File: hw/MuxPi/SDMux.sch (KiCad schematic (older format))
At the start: 14 parts, among them J2 112K-TBA0-RA1, P9 T821108A1S100CEU, Q4 MMBT4403LT1, Q5 MMBT4403LT1, U7 MC74HC1G04DTT1G, U8 TS3A27518EPWR

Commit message: Add detailed info to MuxPi electronic components
The additional information includes manufacturer names and
manufacturer symbols for all components except ceramic capacitors
and resistors. It allows to create BOM (Bill Of Materials) with
actual product names.

Change-Id: Id1c518bba60322d4b8b132ad14261806070abc27
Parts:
- C26: Manufacturer (none) -> AVX; Symbol (none) -> TAJA475K016RNJ
- J2: Manufacturer (none) -> ATTEND; Symbol (none) -> 112K-TBA0-RA1
- P9: Manufacturer (none) -> AMPHENOL; Symbol (none) -> T821108A1S100CEU
- Q4, Q5: Manufacturer (none) -> ON SEMICONDUCTOR; Symbol (none) -> MMBT4403LT1G
- U7: Manufacturer (none) -> ON SEMICONDUCTOR; Symbol (none) -> MC74HC1G04DTT1G
- U8: Manufacturer (none) -> TEXAS INSTRUMENTS; Symbol (none) -> TS3A27518EPWR
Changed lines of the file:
@@
 F 3 "http://www.ti.com/lit/ds/symlink/ts3a27518e.pdf" H 5350 4650 60  0001 C CNN
 F 4 "http://pl.farnell.com/texas-instruments/ts3a27518epwr/ic-6bit-1-of-2-mux-demux-24tssop/dp/1735605" H 5050 4950 60  0001 C CNN "Shop link"
+F 5 "TEXAS INSTRUMENTS" H 5050 4950 50  0001 C CNN "Manufacturer"
+F 6 "TS3A27518EPWR" H 5050 4950 50  0001 C CNN "Symbol"
 	1    5050 4950
 	1    0    0    -1
@@
 F 3 "http://www.tme.eu/pl/Document/0bd9f377abd5f258bb30856efe9f427e/mc74hc1g04.pdf" H 4095 3365 60  0001 C CNN
 F 4 "http://www.tme.eu/pl/details/mc74hc1g04dtt1g/bramki-inwertery/on-semiconductor/" H 3950 3250 60  0001 C CNN "Shop link"
+F 5 "ON SEMICONDUCTOR" H 3950 3250 50  0001 C CNN "Manufacturer"
+F 6 "MC74HC1G04DTT1G" H 3950 3250 50  0001 C CNN "Symbol"
 	1    3950 3250
 	1    0    0    -1
@@
 F 3 "http://www.tme.eu/pl/Document/d9baf2fd66256bac7b840e9a66d44492/112K-TBA0-RA1.pdf" H 6900 4250 60  0001 C CNN
 F 4 "http://www.tme.eu/pl/details/112k-tba0-ra1/zlacza-do-kart/attend/" H 6900 4250 60  0001 C CNN "Shop link"
+F 5 "ATTEND" H 6900 4250 50  0001 C CNN "Manufacturer"
+F 6 "112K-TBA0-RA1" H 6900 4250 50  0001 C CNN "Symbol"
 	1    6900 4250
 	1    0    0    -1
@@
 F 3 "http://www.tme.eu/pl/Document/85f84849ee9dc6997647a15c8c95a9d3/taj.pdf" H 7850 5850 60  0001 C CNN
 F 4 "http://www.tme.eu/pl/details/taja475k016r/kondensatory-tantalowe-smd/avx/taja475k016rnj/" H 7850 5850 60  0001 C CNN "Shop link"
+F 5 "AVX" H 7850 5850 50  0001 C CNN "Manufacturer"
+F 6 "TAJA475K016RNJ" H 7850 5850 50  0001 C CNN "Symbol"
 	1    7850 5850
 	1    0    0    -1
@@
 F 3 "http://www.tme.eu/pl/Document/cda30bae7de800ca9be388e3f3476120/T821-1-08-S1.pdf" H 8850 700 60  0001 C CNN
 F 4 "http://www.tme.eu/pl/details/t821-1-08-s1/zlacza-idc/amphenol/t821108a1s100ceu/" H 8850 1900 60  0001 C CNN "Shop link"
+F 5 "AMPHENOL" H 8850 1900 50  0001 C CNN "Manufacturer"
+F 6 "T821108A1S100CEU" H 8850 1900 50  0001 C CNN "Symbol"
 	1    8850 1900
 	1    0    0    -1
@@
 F 3 "https://www.tme.eu/pl/Document/b8fb0b2a2196eb2b0100116bda4d5a47/mmbt4403.pdf" H 5400 1600 50  0001 L CNN
 F 4 "https://www.tme.eu/pl/details/mmbt4403lt1g/tranzystory-pnp-smd/on-semiconductor/" V 5400 1600 50  0001 C CNN "Shop link"
+F 5 "ON SEMICONDUCTOR" V 5400 1600 50  0001 C CNN "Manufacturer"
+F 6 "MMBT4403LT1G" V 5400 1600 50  0001 C CNN "Symbol"
 	1    5400 1600
-	0    1    -1   0
-$EndComp
-$Comp
-L MuxPi:MMBT4403LT1 Q5
-U 1 1 5A6A2FE1
-P 5400 2650
-F 0 "Q5" V 5728 2650 50  0000 C CNN
-F 1 "MMBT4403LT1" V 5637 2650 50  0000 C CNN
-F 2 "TO_SOT_Packages_SMD:SOT-23" H 5600 2575 50  0001 L CIN
-F 3 "https://www.tme.eu/pl/Document/b8fb0b2a2196eb2b0100116bda4d5a47/mmbt4403.pdf" H 5400 2650 50  0001 L CNN
-F 4 "https://www.tme.eu/pl/details/mmbt4403lt1g/tranzystory-pnp-smd/on-semiconductor/" V 5400 2650 50  0001 C CNN "Shop link"
-	1    5400 2650
 	0    1    -1   0
 $EndComp
@@
 	5400 2200 5400 1850
 Connection ~ 5400 1850
+$Comp
+L MuxPi:MMBT4403LT1 Q5
+U 1 1 5A8F3224
+P 5400 2650
+F 0 "Q5" V 5728 2650 50  0000 C CNN
+F 1 "MMBT4403LT1" V 5637 2650 50  0000 C CNN
+F 2 "TO_SOT_Packages_SMD:SOT-23" H 5600 2575 50  0001 L CIN
+F 3 "https://www.tme.eu/pl/Document/b8fb0b2a2196eb2b0100116bda4d5a47/mmbt4403.pdf" H 5400 2650 50  0001 L CNN
+F 4 "https://www.tme.eu/pl/details/mmbt4403lt1g/tranzystory-pnp-smd/on-semiconductor/" V 5400 2650 50  0001 C CNN "Shop link"
+F 5 "ON SEMICONDUCTOR" V 5400 2650 50  0001 C CNN "Manufacturer"
+F 6 "MMBT4403LT1G" V 5400 2650 50  0001 C CNN "Symbol"
+	1    5400 2650
+	0    1    -1   0
+$EndComp
 $EndSCHEMATC

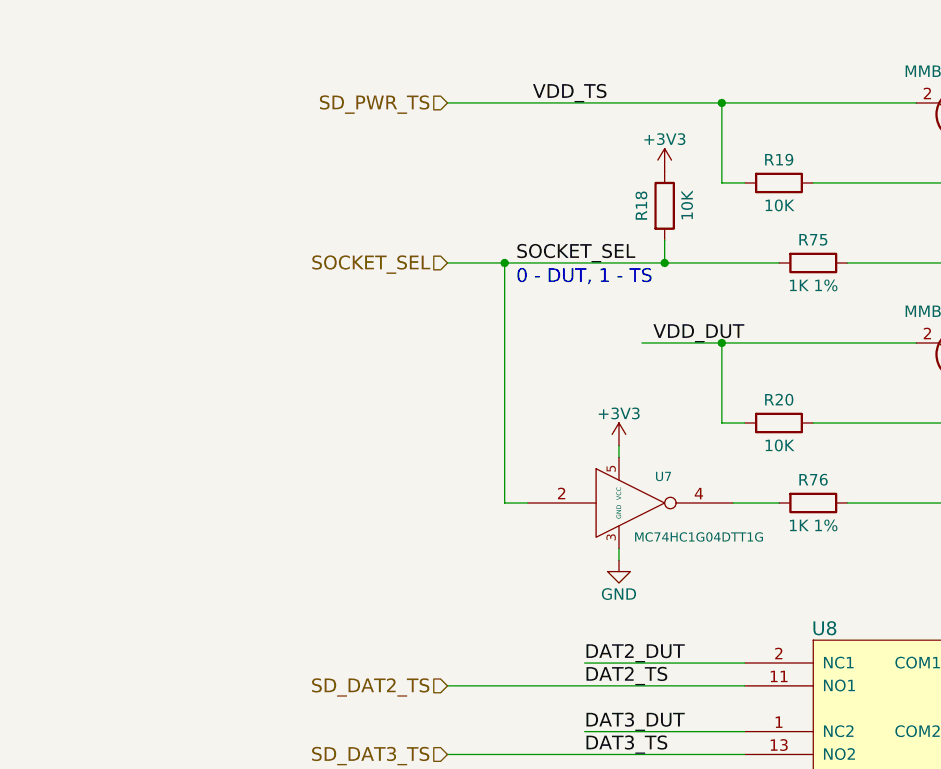
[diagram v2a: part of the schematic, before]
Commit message: Update hardware design to version 1.2
Change-Id: I36445887bfaa5fada88d8bf3915603605de47512
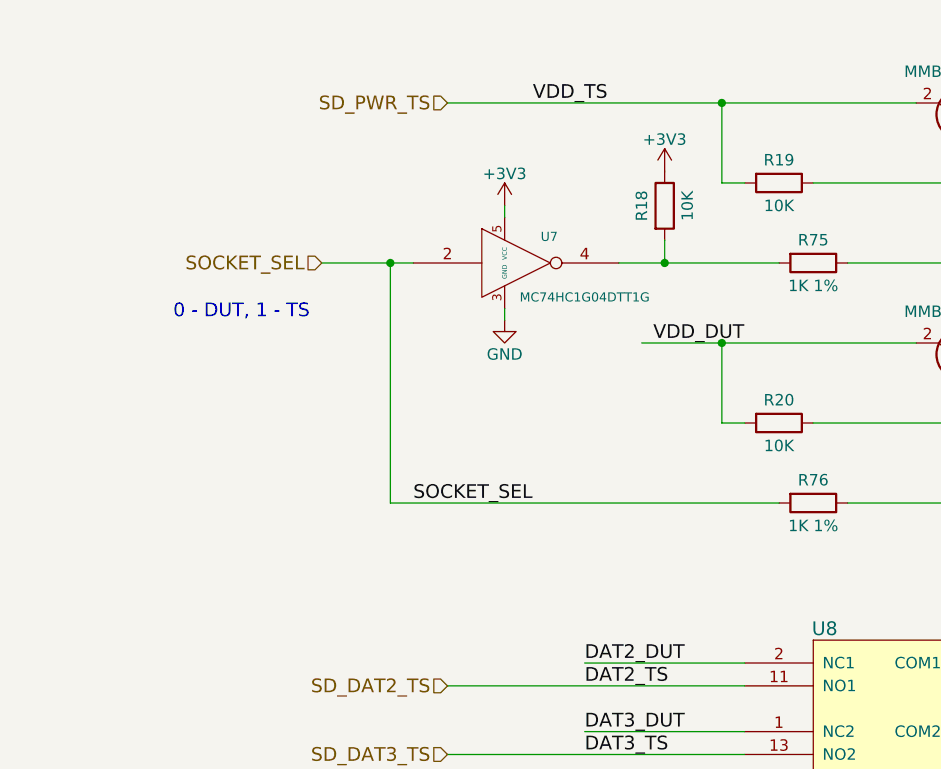
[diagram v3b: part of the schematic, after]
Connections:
- net SOCKET_SEL: now also R76.2; no longer R18.2, R75.2
- net at U7.4: now also R18.2, R75.2; no longer R76.2
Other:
- moved on the sheet: U7
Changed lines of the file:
@@
 EESchema Schematic File Version 4
+LIBS:MuxPi-cache
 EELAYER 26 0
 EELAYER END
@@
 encoding utf-8
 Sheet 7 12
-Title ""
-Date ""
-Rev ""
-Comp ""
-Comment1 ""
-Comment2 ""
+Title "MuxPi"
+Date "2018-04-20"
+Rev "1.2"
+Comp "SRPOL"
+Comment1 "Author: Adam Malinowski <a.malinowsk2@partner.samsung.com>"
+Comment2 "Copyright (c) 2016 - 2018 Samsung Electronics Co., Ltd All Rights Reserved"
 Comment3 ""
 Comment4 ""
@@
 L MuxPi:74AHC1G14 U7
 U 1 1 584BAD12
-P 3950 3250
+P 3450 2200
 AR Path="/584BAD12" Ref="U7"  Part="1"
 AR Path="/584BA053/584BAD12" Ref="U7"  Part="1"
-F 0 "U7" H 4095 3365 40  0000 C CNN
-F 1 "MC74HC1G04DTT1G" H 4250 3100 40  0000 C CNN
-F 2 "TO_SOT_Packages_SMD:SOT-23-5" H 4045 3115 30  0001 C CNN
-F 3 "http://www.tme.eu/pl/Document/0bd9f377abd5f258bb30856efe9f427e/mc74hc1g04.pdf" H 4095 3365 60  0001 C CNN
-F 4 "http://www.tme.eu/pl/details/mc74hc1g04dtt1g/bramki-inwertery/on-semiconductor/" H 3950 3250 60  0001 C CNN "Shop link"
-F 5 "ON SEMICONDUCTOR" H 3950 3250 50  0001 C CNN "Manufacturer"
-F 6 "MC74HC1G04DTT1G" H 3950 3250 50  0001 C CNN "Symbol"
-	1    3950 3250
+F 0 "U7" H 3595 2315 40  0000 C CNN
+F 1 "MC74HC1G04DTT1G" H 3750 2050 40  0000 C CNN
+F 2 "TO_SOT_Packages_SMD:SOT-23-5" H 3545 2065 30  0001 C CNN
+F 3 "http://www.tme.eu/pl/Document/0bd9f377abd5f258bb30856efe9f427e/mc74hc1g04.pdf" H 3595 2315 60  0001 C CNN
+F 4 "http://www.tme.eu/pl/details/mc74hc1g04dtt1g/bramki-inwertery/on-semiconductor/" H 3450 2200 60  0001 C CNN "Shop link"
+F 5 "ON SEMICONDUCTOR" H 3450 2200 50  0001 C CNN "Manufacturer"
+F 6 "MC74HC1G04DTT1G" H 3450 2200 50  0001 C CNN "Symbol"
+	1    3450 2200
 	1    0    0    -1
 $EndComp
 Text Label 4050 2550 0    60   ~ 0
 VDD_DUT
-Text Notes 3450 2300 0    60   ~ 0
+Text Notes 1950 2450 0    60   ~ 0
 0 - DUT, 1 - TS
 $Comp
@@
 L MuxPi:GND #PWR082
 U 1 1 584BAD22
-P 3900 3500
-F 0 "#PWR082" H 3900 3250 50  0001 C CNN
-F 1 "GND" H 3900 3350 50  0000 C CNN
-F 2 "" H 3900 3500 60  0000 C CNN
-F 3 "" H 3900 3500 60  0000 C CNN
-	1    3900 3500
+P 3400 2450
+F 0 "#PWR082" H 3400 2200 50  0001 C CNN
+F 1 "GND" H 3400 2300 50  0000 C CNN
+F 2 "" H 3400 2450 60  0000 C CNN
+F 3 "" H 3400 2450 60  0000 C CNN
+	1    3400 2450
 	-1   0    0    -1
 $EndComp
@@
 L MuxPi:+3V3 #PWR081
 U 1 1 584BAD80
-P 3900 3000
-F 0 "#PWR081" H 3900 2850 50  0001 C CNN
-F 1 "+3V3" H 3900 3140 50  0000 C CNN
-F 2 "" H 3900 3000 60  0000 C CNN
-F 3 "" H 3900 3000 60  0000 C CNN
-	1    3900 3000
-	1    0    0    -1
-$EndComp
-Text Label 3450 2200 0    60   ~ 0
+P 3400 1950
+F 0 "#PWR081" H 3400 1800 50  0001 C CNN
+F 1 "+3V3" H 3400 2090 50  0000 C CNN
+F 2 "" H 3400 1950 60  0000 C CNN
+F 3 "" H 3400 1950 60  0000 C CNN
+	1    3400 1950
+	1    0    0    -1
+$EndComp
+Text Label 3000 3250 0    60   ~ 0
 SOCKET_SEL
 $Comp
@@
 Text Label 7500 5550 0    60   ~ 0
 USD_VDD
-Text HLabel 3150 2200 0    60   Input ~ 0
+Text HLabel 2600 2200 0    60   Input ~ 0
 SOCKET_SEL
 Text HLabel 3150 1500 0    60   Input ~ 0
@@
 	4350 5950 4350 6050
 Wire Wire Line
-	3900 3450 3900 3500
-Wire Wire Line
-	3900 3000 3900 3050
+	3400 2400 3400 2450
+Wire Wire Line
+	3400 1950 3400 2000
 Wire Wire Line
 	4450 5450 3750 5450
@@
 Wire Wire Line
 	9200 1950 9200 2150
-Connection ~ 4100 2200
 Wire Wire Line
 	3750 5750 4350 5750
@@
 Connection ~ 5800 2050
 Wire Wire Line
-	4400 3250 4600 3250
-Wire Wire Line
-	3150 2200 3400 2200
-Wire Wire Line
-	3500 3250 3400 3250
-Connection ~ 3400 2200
+	2600 2200 2900 2200
 Wire Wire Line
 	6300 2050 6300 3800
@@
 	5750 3950 5750 4450
 Wire Wire Line
-	3400 3250 3400 2200
+	2900 3250 2900 2200
 Wire Wire Line
 	5850 3950 5850 4250
@@
 Wire Wire Line
 	5800 2050 5800 2550
-Wire Wire Line
-	3400 2200 4100 2200
 Wire Wire Line
 	7500 5650 7500 5700
@@
 	0    1    -1   0
 $EndComp
+Wire Wire Line
+	2900 2200 3000 2200
+Connection ~ 2900 2200
+Wire Wire Line
+	3900 2200 4100 2200
+Connection ~ 4100 2200
+Wire Wire Line
+	2900 3250 4600 3250
 $EndSCHEMATC

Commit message: Update  hardware design to version 1.4
Change-Id: I72a4381d8bec5616bc1cfe04dc8a5407141c77d5
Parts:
- P9: footprint w_conn_strip:vasch_strip_4x2 -> MuxPi:vasch_strip_4x2
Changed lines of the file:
@@
 EESchema Schematic File Version 4
 LIBS:MuxPi-cache
-EELAYER 26 0
+EELAYER 29 0
 EELAYER END
 $Descr A4 11693 8268
@@
 Sheet 7 12
 Title "MuxPi"
-Date "2018-08-14"
-Rev "1.3"
+Date "2018-11-16"
+Rev "1.4"
 Comp "SRPOL"
 Comment1 "Author: Adam Malinowski <a.malinowsk2@partner.samsung.com>"
@@
 F 0 "P9" H 8850 2150 50  0000 C CNN
 F 1 "T821108A1S100CEU" H 8850 2250 50  0000 C CNN
-F 2 "w_conn_strip:vasch_strip_4x2" H 8850 700 60  0001 C CNN
+F 2 "MuxPi:vasch_strip_4x2" H 8850 700 60  0001 C CNN
 F 3 "http://www.tme.eu/pl/Document/cda30bae7de800ca9be388e3f3476120/T821-1-08-S1.pdf" H 8850 700 60  0001 C CNN
 F 4 "http://www.tme.eu/pl/details/t821-1-08-s1/zlacza-idc/amphenol/t821108a1s100ceu/" H 8850 1900 60  0001 C CNN "Shop link"
